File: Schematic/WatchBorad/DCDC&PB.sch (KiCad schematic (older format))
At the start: 21 parts, among them M1 Motor_DC, SW3 SW_Push, SW4 SW_Push, SW5 SW_Push, U10 TPS62740DSST, U9 MAX809STRG

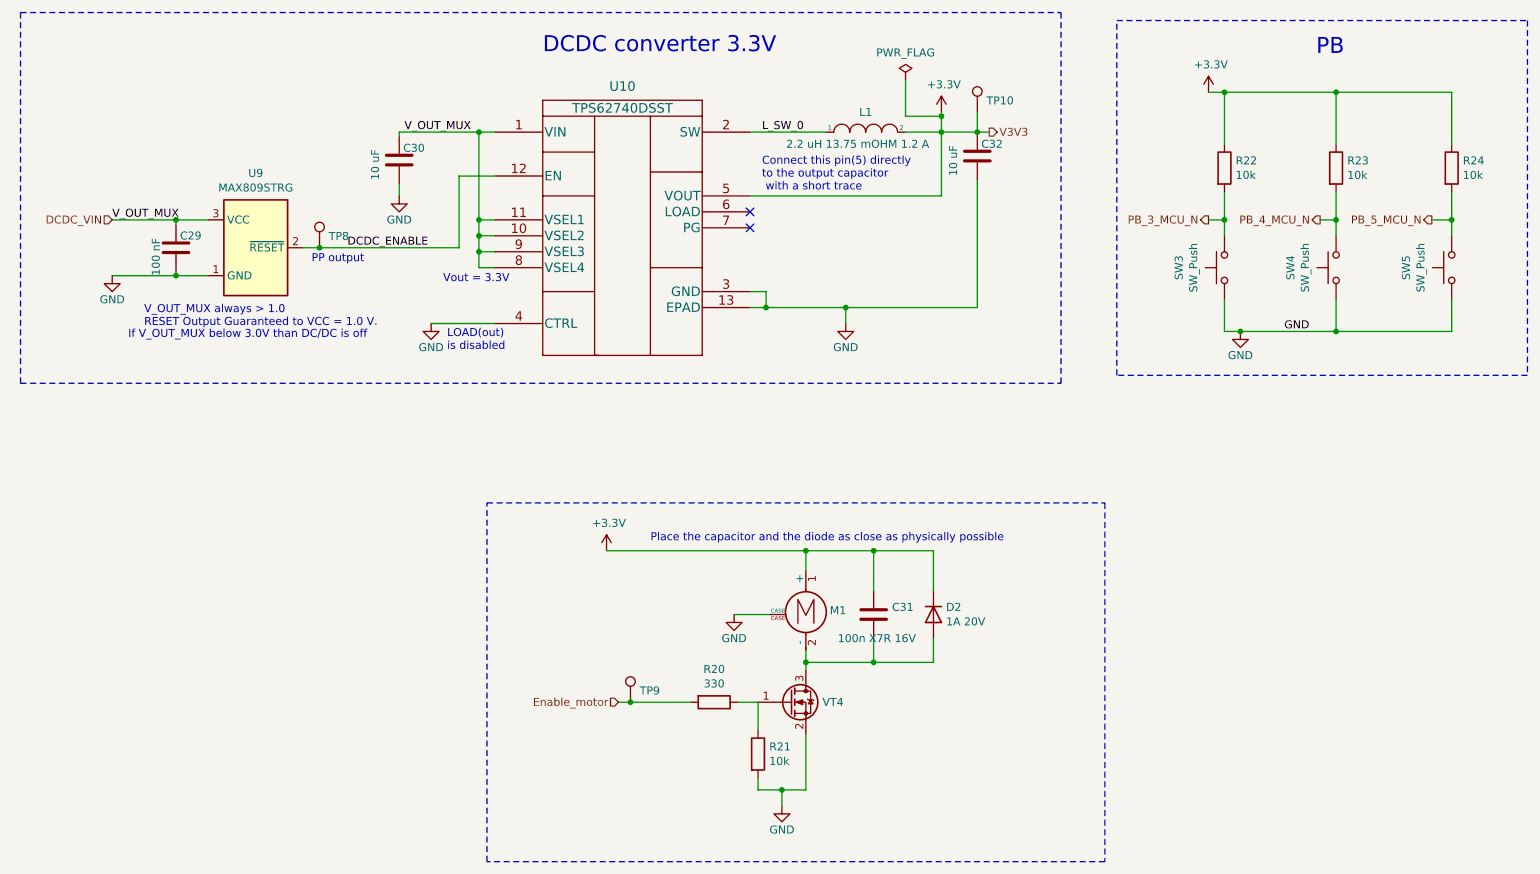
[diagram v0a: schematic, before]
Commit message: PBs are modified to one logic. Some minot changes
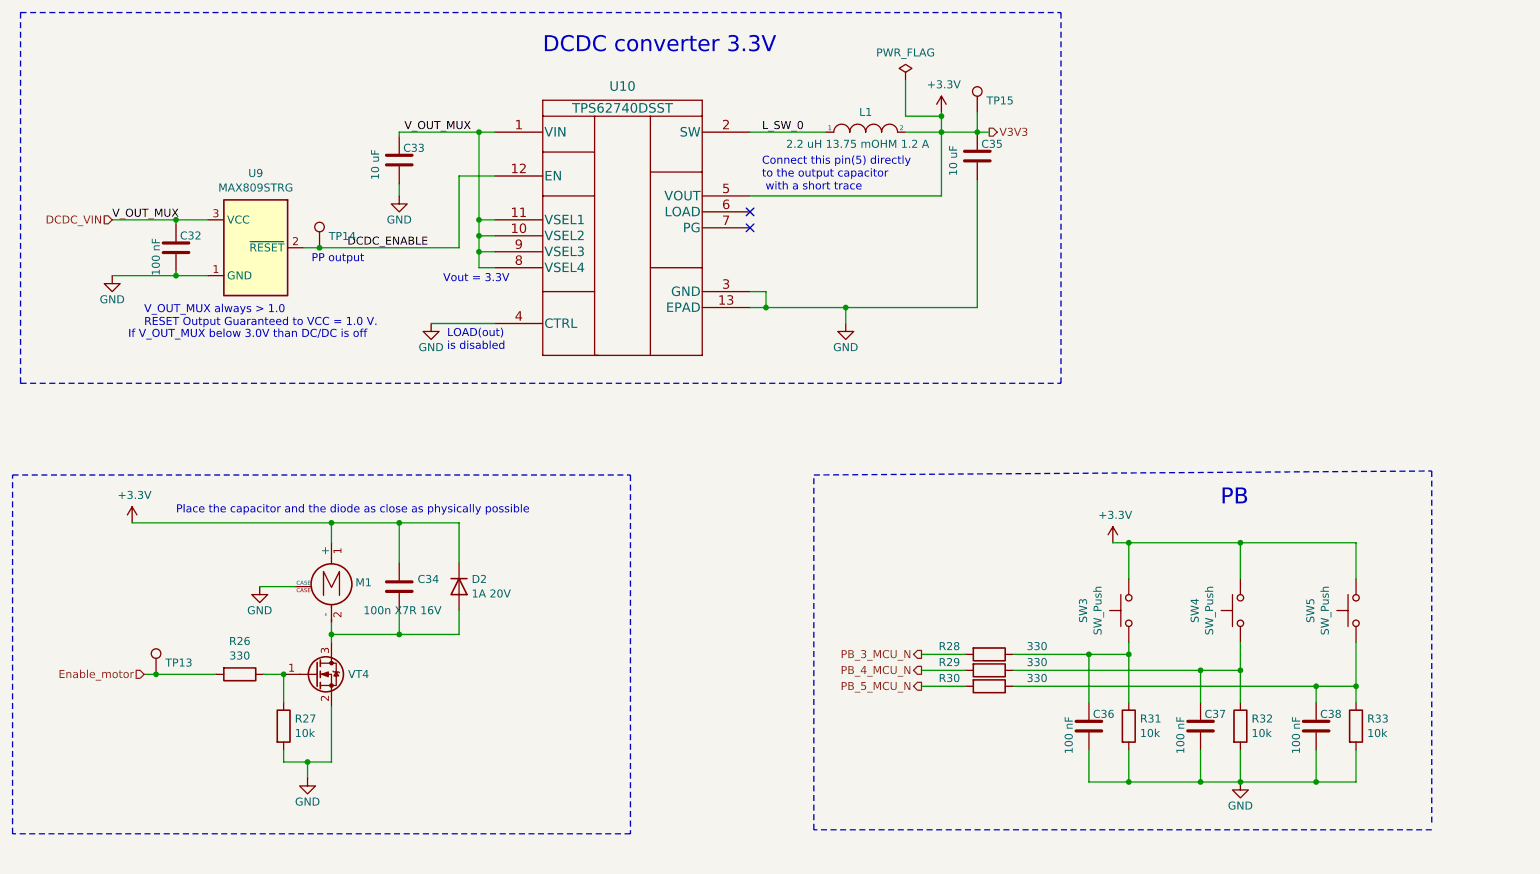
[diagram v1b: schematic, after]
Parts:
- added C36, C37, C38: 100 nF, Capacitors_SMD:C_0603_HandSoldering, symbol Device:C
- added R28, R29, R30: 330, Resistors_SMD:R_0603_HandSoldering, symbol Device:R
- renumbered C29 to C32, C30 to C33, C31 to C34, C32 to C35, R20 to R26, R21 to R27, R22 to R31, R23 to R32, R24 to R33, TP9 to TP13, TP8 to TP14, TP10 to TP15
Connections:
- net +3V3: now also SW3.2, SW4.2, SW5.2; no longer R31.1, R32.1, R33.1
- net GND: now also R31.2, R32.2, R33.2, C36.2, C37.2, C38.2; no longer SW3.1, SW4.1, SW5.1
- net PB_3_MCU_N: now also R28.2; no longer R31.2, SW3.2
- net PB_4_MCU_N: now also R29.2; no longer R32.2, SW4.2
- net PB_5_MCU_N: now also R30.2; no longer R33.2, SW5.2
- new net: C36.1, R28.1, R31.1, SW3.1
- new net: C37.1, R29.1, R32.1, SW4.1
- new net: C38.1, R30.1, R33.1, SW5.1
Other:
- moved on the sheet: C34, D2, M1, R26, R27, R31, R32, R33, SW3, SW4, SW5, TP13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

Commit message: Fixed LCSC schematic link :Schematic [SCHEMATIC]
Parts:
- C33, C35: LCSC https://lcsc.com/product-detail/Multilayer-Ceramic-Capacito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 -> (none); lcsc (none) -> https://lcsc.com/product-detail/Multilayer-Ceramic-Capacito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
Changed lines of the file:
@@
 AR Path="/5F7F86D0/5F9A3890" Ref="U?"  Part="1"
 AR Path="/5F988DA5/5F9A3890" Ref="U10"  Part="1"
+AR Path="/5F9A3890" Ref="U10"  Part="1"
 F 0 "U10" H 4800 2262 60  0000 C CNN
 F 1 "TPS62740DSST" H 4800 2125 60  0000 C CNN
@@
 F 2 "Capacitors_SMD:C_0603_HandSoldering" H 3438 1800 50  0001 C CNN
 F 3 "~" H 3400 1950 50  0001 C CNN
-F 4 "https://lcsc.com/product-detail/Multilayer-Ceramic-Capacitors-MLCC-SMD-SMT_SANYEAR-C0603X5R106M160NT_C466781.html" H 3400 1950 50  0001 C CNN "LCSC"
+F 4 "" H 3400 1950 50  0001 C CNN "LCSC"
+F 5 "https://lcsc.com/product-detail/Multilayer-Ceramic-Capacitors-MLCC-SMD-SMT_SANYEAR-C0603X5R106M160NT_C466781.html" H 3400 1950 50  0001 C CNN "lcsc"
 	1    3400 1950
 	1    0    0    -1
@@
 F 2 "Capacitors_SMD:C_0603_HandSoldering" H 7063 1775 50  0001 C CNN
 F 3 "~" H 7025 1925 50  0001 C CNN
-F 4 "https://lcsc.com/product-detail/Multilayer-Ceramic-Capacitors-MLCC-SMD-SMT_SANYEAR-C0603X5R106M160NT_C466781.html" H 7025 1925 50  0001 C CNN "LCSC"
+F 4 "" H 7025 1925 50  0001 C CNN "LCSC"
+F 5 "https://lcsc.com/product-detail/Multilayer-Ceramic-Capacitors-MLCC-SMD-SMT_SANYEAR-C0603X5R106M160NT_C466781.html" H 7025 1925 50  0001 C CNN "lcsc"
 	1    7025 1925
 	1    0    0    -1

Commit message: Added footpring for GC9A01 display. Fixed display lines(FMARK->DC)
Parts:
- U10: symbol DCDC_Local:TPS62740DSST -> WatchBorad-rescue:TPS62740DSST-DCDC_Local
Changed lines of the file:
@@
 $EndDescr
 $Comp
-L DCDC_Local:TPS62740DSST U?
+L WatchBorad-rescue:TPS62740DSST-DCDC_Local U?
 U 1 1 5F9A3890
 P 4000 1875

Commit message: Fixed components references for 0603 resistors and capacitors[SCHEMATIC]
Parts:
- C32, C33, C34, C35, C36, C37, C38: footprint Capacitors_SMD:C_0603_HandSoldering -> Capacitor_SMD:C_0603_1608Metric_Pad1.08x0.95mm_HandSolder
- R26, R27, R28, R29, R30, R31, R32, R33: footprint Resistors_SMD:R_0603_HandSoldering -> Resistor_SMD:R_0603_1608Metric_Pad0.98x0.95mm_HandSolder
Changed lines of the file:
@@
 F 0 "C33" H 3425 2025 50  0000 L CNN
 F 1 "10 uF" V 3250 1825 50  0000 L CNN
-F 2 "Capacitors_SMD:C_0603_HandSoldering" H 3438 1800 50  0001 C CNN
+F 2 "Capacitor_SMD:C_0603_1608Metric_Pad1.08x0.95mm_HandSolder" H 3438 1800 50  0001 C CNN
 F 3 "~" H 3400 1950 50  0001 C CNN
 F 4 "" H 3400 1950 50  0001 C CNN "LCSC"
@@
 F 0 "C35" H 7050 2000 50  0000 L CNN
 F 1 "10 uF" V 6875 1800 50  0000 L CNN
-F 2 "Capacitors_SMD:C_0603_HandSoldering" H 7063 1775 50  0001 C CNN
+F 2 "Capacitor_SMD:C_0603_1608Metric_Pad1.08x0.95mm_HandSolder" H 7063 1775 50  0001 C CNN
 F 3 "~" H 7025 1925 50  0001 C CNN
 F 4 "" H 7025 1925 50  0001 C CNN "LCSC"
@@
 F 0 "C32" H 2025 2575 50  0000 L CNN
 F 1 "100 nF" V 1875 2325 50  0000 L CNN
-F 2 "Capacitors_SMD:C_0603_HandSoldering" H 2038 2350 50  0001 C CNN
+F 2 "Capacitor_SMD:C_0603_1608Metric_Pad1.08x0.95mm_HandSolder" H 2038 2350 50  0001 C CNN
 F 3 "~" H 2000 2500 50  0001 C CNN
 	1    2000 2500
@@
 F 0 "R31" H 8045 5546 50  0000 L CNN
 F 1 "10k" H 8045 5455 50  0000 L CNN
-F 2 "Resistors_SMD:R_0603_HandSoldering" V 7905 5500 50  0001 C CNN
+F 2 "Resistor_SMD:R_0603_1608Metric_Pad0.98x0.95mm_HandSolder" V 7905 5500 50  0001 C CNN
 F 3 "~" H 7975 5500 50  0001 C CNN
 	1    7975 5500
@@
 F 0 "R32" H 8745 5546 50  0000 L CNN
 F 1 "10k" H 8745 5455 50  0000 L CNN
-F 2 "Resistors_SMD:R_0603_HandSoldering" V 8605 5500 50  0001 C CNN
+F 2 "Resistor_SMD:R_0603_1608Metric_Pad0.98x0.95mm_HandSolder" V 8605 5500 50  0001 C CNN
 F 3 "~" H 8675 5500 50  0001 C CNN
 	1    8675 5500
@@
 F 0 "R33" H 9470 5546 50  0000 L CNN
 F 1 "10k" H 9470 5455 50  0000 L CNN
-F 2 "Resistors_SMD:R_0603_HandSoldering" V 9330 5500 50  0001 C CNN
+F 2 "Resistor_SMD:R_0603_1608Metric_Pad0.98x0.95mm_HandSolder" V 9330 5500 50  0001 C CNN
 F 3 "~" H 9400 5500 50  0001 C CNN
 	1    9400 5500
@@
 F 0 "R27" H 2745 5546 50  0000 L CNN
 F 1 "10k" H 2745 5455 50  0000 L CNN
-F 2 "Resistors_SMD:R_0603_HandSoldering" V 2605 5500 50  0001 C CNN
+F 2 "Resistor_SMD:R_0603_1608Metric_Pad0.98x0.95mm_HandSolder" V 2605 5500 50  0001 C CNN
 F 3 "~" H 2675 5500 50  0001 C CNN
 	1    2675 5500
@@
 F 0 "R26" V 2193 5175 50  0000 C CNN
 F 1 "330" V 2284 5175 50  0000 C CNN
-F 2 "Resistors_SMD:R_0603_HandSoldering" V 2330 5175 50  0001 C CNN
+F 2 "Resistor_SMD:R_0603_1608Metric_Pad0.98x0.95mm_HandSolder" V 2330 5175 50  0001 C CNN
 F 3 "https://lcsc.com/product-detail/Others_Viking-Tech-ARG03FTC3300_C217969.html" H 2400 5175 50  0001 C CNN
 	1    2400 5175
@@
 F 0 "C34" H 3515 4671 50  0000 L CNN
 F 1 "100n X7R 16V" H 3175 4475 50  0000 L CNN
-F 2 "Capacitors_SMD:C_0603_HandSoldering" H 3438 4475 50  0001 C CNN
+F 2 "Capacitor_SMD:C_0603_1608Metric_Pad1.08x0.95mm_HandSolder" H 3438 4475 50  0001 C CNN
 F 3 "~" H 3400 4625 50  0001 C CNN
 	1    3400 4625
@@
 F 0 "R28" V 7050 4800 50  0000 C CNN
 F 1 "330" V 7050 5350 50  0000 C CNN
-F 2 "Resistors_SMD:R_0603_HandSoldering" V 7030 5050 50  0001 C CNN
+F 2 "Resistor_SMD:R_0603_1608Metric_Pad0.98x0.95mm_HandSolder" V 7030 5050 50  0001 C CNN
 F 3 "https://lcsc.com/product-detail/Others_Viking-Tech-ARG03FTC3300_C217969.html" H 7100 5050 50  0001 C CNN
 	1    7100 5050
@@
 F 0 "R29" V 7050 4900 50  0000 C CNN
 F 1 "330" V 7050 5450 50  0000 C CNN
-F 2 "Resistors_SMD:R_0603_HandSoldering" V 7030 5150 50  0001 C CNN
+F 2 "Resistor_SMD:R_0603_1608Metric_Pad0.98x0.95mm_HandSolder" V 7030 5150 50  0001 C CNN
 F 3 "https://lcsc.com/product-detail/Others_Viking-Tech-ARG03FTC3300_C217969.html" H 7100 5150 50  0001 C CNN
 	1    7100 5150
@@
 F 0 "R30" V 7050 5000 50  0000 C CNN
 F 1 "330" V 7050 5550 50  0000 C CNN
-F 2 "Resistors_SMD:R_0603_HandSoldering" V 7030 5250 50  0001 C CNN
+F 2 "Resistor_SMD:R_0603_1608Metric_Pad0.98x0.95mm_HandSolder" V 7030 5250 50  0001 C CNN
 F 3 "https://lcsc.com/product-detail/Others_Viking-Tech-ARG03FTC3300_C217969.html" H 7100 5250 50  0001 C CNN
 	1    7100 5250
@@
 F 0 "C36" H 7750 5575 50  0000 L CNN
 F 1 "100 nF" V 7600 5325 50  0000 L CNN
-F 2 "Capacitors_SMD:C_0603_HandSoldering" H 7763 5350 50  0001 C CNN
+F 2 "Capacitor_SMD:C_0603_1608Metric_Pad1.08x0.95mm_HandSolder" H 7763 5350 50  0001 C CNN
 F 3 "~" H 7725 5500 50  0001 C CNN
 	1    7725 5500
@@
 F 0 "C37" H 8450 5575 50  0000 L CNN
 F 1 "100 nF" V 8300 5325 50  0000 L CNN
-F 2 "Capacitors_SMD:C_0603_HandSoldering" H 8463 5350 50  0001 C CNN
+F 2 "Capacitor_SMD:C_0603_1608Metric_Pad1.08x0.95mm_HandSolder" H 8463 5350 50  0001 C CNN
 F 3 "~" H 8425 5500 50  0001 C CNN
 	1    8425 5500
@@
 F 0 "C38" H 9175 5575 50  0000 L CNN
 F 1 "100 nF" V 9025 5325 50  0000 L CNN
-F 2 "Capacitors_SMD:C_0603_HandSoldering" H 9188 5350 50  0001 C CNN
+F 2 "Capacitor_SMD:C_0603_1608Metric_Pad1.08x0.95mm_HandSolder" H 9188 5350 50  0001 C CNN
 F 3 "~" H 9150 5500 50  0001 C CNN
 	1    9150 5500

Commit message: Updated 0603 components from hand-solder version to fabrical
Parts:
- C32, C33, C34, C35, C36, C37, C38: footprint Capacitor_SMD:C_0603_1608Metric_Pad1.08x0.95mm_HandSolder -> Capacitor_SMD:C_0603_1608Metric
- R26, R27, R28, R29, R30, R31, R32, R33: footprint Resistor_SMD:R_0603_1608Metric_Pad0.98x0.95mm_HandSolder -> Resistor_SMD:R_0603_1608Metric
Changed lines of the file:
@@
 F 0 "C33" H 3425 2025 50  0000 L CNN
 F 1 "10 uF" V 3250 1825 50  0000 L CNN
-F 2 "Capacitor_SMD:C_0603_1608Metric_Pad1.08x0.95mm_HandSolder" H 3438 1800 50  0001 C CNN
+F 2 "Capacitor_SMD:C_0603_1608Metric" H 3438 1800 50  0001 C CNN
 F 3 "~" H 3400 1950 50  0001 C CNN
 F 4 "" H 3400 1950 50  0001 C CNN "LCSC"
@@
 F 0 "C35" H 7050 2000 50  0000 L CNN
 F 1 "10 uF" V 6875 1800 50  0000 L CNN
-F 2 "Capacitor_SMD:C_0603_1608Metric_Pad1.08x0.95mm_HandSolder" H 7063 1775 50  0001 C CNN
+F 2 "Capacitor_SMD:C_0603_1608Metric" H 7063 1775 50  0001 C CNN
 F 3 "~" H 7025 1925 50  0001 C CNN
 F 4 "" H 7025 1925 50  0001 C CNN "LCSC"
@@
 F 0 "C32" H 2025 2575 50  0000 L CNN
 F 1 "100 nF" V 1875 2325 50  0000 L CNN
-F 2 "Capacitor_SMD:C_0603_1608Metric_Pad1.08x0.95mm_HandSolder" H 2038 2350 50  0001 C CNN
+F 2 "Capacitor_SMD:C_0603_1608Metric" H 2038 2350 50  0001 C CNN
 F 3 "~" H 2000 2500 50  0001 C CNN
 	1    2000 2500
@@
 F 0 "R31" H 8045 5546 50  0000 L CNN
 F 1 "10k" H 8045 5455 50  0000 L CNN
-F 2 "Resistor_SMD:R_0603_1608Metric_Pad0.98x0.95mm_HandSolder" V 7905 5500 50  0001 C CNN
+F 2 "Resistor_SMD:R_0603_1608Metric" V 7905 5500 50  0001 C CNN
 F 3 "~" H 7975 5500 50  0001 C CNN
 	1    7975 5500
@@
 F 0 "R32" H 8745 5546 50  0000 L CNN
 F 1 "10k" H 8745 5455 50  0000 L CNN
-F 2 "Resistor_SMD:R_0603_1608Metric_Pad0.98x0.95mm_HandSolder" V 8605 5500 50  0001 C CNN
+F 2 "Resistor_SMD:R_0603_1608Metric" V 8605 5500 50  0001 C CNN
 F 3 "~" H 8675 5500 50  0001 C CNN
 	1    8675 5500
@@
 F 0 "R33" H 9470 5546 50  0000 L CNN
 F 1 "10k" H 9470 5455 50  0000 L CNN
-F 2 "Resistor_SMD:R_0603_1608Metric_Pad0.98x0.95mm_HandSolder" V 9330 5500 50  0001 C CNN
+F 2 "Resistor_SMD:R_0603_1608Metric" V 9330 5500 50  0001 C CNN
 F 3 "~" H 9400 5500 50  0001 C CNN
 	1    9400 5500
@@
 F 0 "R27" H 2745 5546 50  0000 L CNN
 F 1 "10k" H 2745 5455 50  0000 L CNN
-F 2 "Resistor_SMD:R_0603_1608Metric_Pad0.98x0.95mm_HandSolder" V 2605 5500 50  0001 C CNN
+F 2 "Resistor_SMD:R_0603_1608Metric" V 2605 5500 50  0001 C CNN
 F 3 "~" H 2675 5500 50  0001 C CNN
 	1    2675 5500
@@
 F 0 "R26" V 2193 5175 50  0000 C CNN
 F 1 "330" V 2284 5175 50  0000 C CNN
-F 2 "Resistor_SMD:R_0603_1608Metric_Pad0.98x0.95mm_HandSolder" V 2330 5175 50  0001 C CNN
+F 2 "Resistor_SMD:R_0603_1608Metric" V 2330 5175 50  0001 C CNN
 F 3 "https://lcsc.com/product-detail/Others_Viking-Tech-ARG03FTC3300_C217969.html" H 2400 5175 50  0001 C CNN
 	1    2400 5175
@@
 F 0 "C34" H 3515 4671 50  0000 L CNN
 F 1 "100n X7R 16V" H 3175 4475 50  0000 L CNN
-F 2 "Capacitor_SMD:C_0603_1608Metric_Pad1.08x0.95mm_HandSolder" H 3438 4475 50  0001 C CNN
+F 2 "Capacitor_SMD:C_0603_1608Metric" H 3438 4475 50  0001 C CNN
 F 3 "~" H 3400 4625 50  0001 C CNN
 	1    3400 4625
@@
 F 0 "R28" V 7050 4800 50  0000 C CNN
 F 1 "330" V 7050 5350 50  0000 C CNN
-F 2 "Resistor_SMD:R_0603_1608Metric_Pad0.98x0.95mm_HandSolder" V 7030 5050 50  0001 C CNN
+F 2 "Resistor_SMD:R_0603_1608Metric" V 7030 5050 50  0001 C CNN
 F 3 "https://lcsc.com/product-detail/Others_Viking-Tech-ARG03FTC3300_C217969.html" H 7100 5050 50  0001 C CNN
 	1    7100 5050
@@
 F 0 "R29" V 7050 4900 50  0000 C CNN
 F 1 "330" V 7050 5450 50  0000 C CNN
-F 2 "Resistor_SMD:R_0603_1608Metric_Pad0.98x0.95mm_HandSolder" V 7030 5150 50  0001 C CNN
+F 2 "Resistor_SMD:R_0603_1608Metric" V 7030 5150 50  0001 C CNN
 F 3 "https://lcsc.com/product-detail/Others_Viking-Tech-ARG03FTC3300_C217969.html" H 7100 5150 50  0001 C CNN
 	1    7100 5150
@@
 F 0 "R30" V 7050 5000 50  0000 C CNN
 F 1 "330" V 7050 5550 50  0000 C CNN
-F 2 "Resistor_SMD:R_0603_1608Metric_Pad0.98x0.95mm_HandSolder" V 7030 5250 50  0001 C CNN
+F 2 "Resistor_SMD:R_0603_1608Metric" V 7030 5250 50  0001 C CNN
 F 3 "https://lcsc.com/product-detail/Others_Viking-Tech-ARG03FTC3300_C217969.html" H 7100 5250 50  0001 C CNN
 	1    7100 5250
@@
 F 0 "C36" H 7750 5575 50  0000 L CNN
 F 1 "100 nF" V 7600 5325 50  0000 L CNN
-F 2 "Capacitor_SMD:C_0603_1608Metric_Pad1.08x0.95mm_HandSolder" H 7763 5350 50  0001 C CNN
+F 2 "Capacitor_SMD:C_0603_1608Metric" H 7763 5350 50  0001 C CNN
 F 3 "~" H 7725 5500 50  0001 C CNN
 	1    7725 5500
@@
 F 0 "C37" H 8450 5575 50  0000 L CNN
 F 1 "100 nF" V 8300 5325 50  0000 L CNN
-F 2 "Capacitor_SMD:C_0603_1608Metric_Pad1.08x0.95mm_HandSolder" H 8463 5350 50  0001 C CNN
+F 2 "Capacitor_SMD:C_0603_1608Metric" H 8463 5350 50  0001 C CNN
 F 3 "~" H 8425 5500 50  0001 C CNN
 	1    8425 5500
@@
 F 0 "C38" H 9175 5575 50  0000 L CNN
 F 1 "100 nF" V 9025 5325 50  0000 L CNN
-F 2 "Capacitor_SMD:C_0603_1608Metric_Pad1.08x0.95mm_HandSolder" H 9188 5350 50  0001 C CNN
+F 2 "Capacitor_SMD:C_0603_1608Metric" H 9188 5350 50  0001 C CNN
 F 3 "~" H 9150 5500 50  0001 C CNN
 	1    9150 5500

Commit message: Updated parts list accroding to the Ruslan fixes
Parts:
- D2: lcsc https://lcsc.com/product-detail/Schottky-Barrier-Diodes-SBD_Shandong-Jingdao-Microelectronics-SS12_C353243.html -> https://lcsc.com/product-detail/Schottky-Barrier-Diodes-SBD_Slkor-SLKORMICRO-Elec-SS12_C513476.html
- SW3, SW4, SW5: footprint Buttons_Switches_SMD:SW_SPST_B3U-3000P-B -> OmronSwitch:SW_B3U-3000P; lcsc https://lcsc.com/products/Tactile-Switches_427.html?q=b3u-3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 -> https://lcsc.com/product-detail/Tactile-Switches_Omron-Elec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
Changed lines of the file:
@@
 F 0 "SW3" H 7975 5060 50  0000 C CNN
 F 1 "SW_Push" H 7975 4969 50  0000 C CNN
-F 2 "Buttons_Switches_SMD:SW_SPST_B3U-3000P-B" H 7975 4975 50  0001 C CNN
-F 3 "https://datasheet.lcsc.com/szlcsc/Omron-Electronics-B3U-3000PM-B_C306884.pdf" H 7975 4975 50  0001 C CNN
-F 4 "https://lcsc.com/products/Tactile-Switches_427.html?q=b3u-3000" H 7975 4775 50  0001 C CNN "lcsc"
+F 2 "OmronSwitch:SW_B3U-3000P" H 7975 4975 50  0001 C CNN
+F 3 "https://datasheet.lcsc.com/lcsc/2012042009_Omron-Electronics-B3U-3000P_C963349.pdf" H 7975 4975 50  0001 C CNN
+F 4 "https://lcsc.com/product-detail/Tactile-Switches_Omron-Electronics-B3U-3000P_C963349.html" H 7975 4775 50  0001 C CNN "lcsc"
 	1    7975 4775
 	0    -1   -1   0
@@
 F 0 "SW4" H 8675 5060 50  0000 C CNN
 F 1 "SW_Push" H 8675 4969 50  0000 C CNN
-F 2 "Buttons_Switches_SMD:SW_SPST_B3U-3000P-B" H 8675 4975 50  0001 C CNN
-F 3 "https://datasheet.lcsc.com/szlcsc/Omron-Electronics-B3U-3000PM-B_C306884.pdf" H 8675 4975 50  0001 C CNN
-F 4 "https://lcsc.com/products/Tactile-Switches_427.html?q=b3u-3000" H 8675 4775 50  0001 C CNN "lcsc"
+F 2 "OmronSwitch:SW_B3U-3000P" H 8675 4975 50  0001 C CNN
+F 3 "https://datasheet.lcsc.com/lcsc/2012042009_Omron-Electronics-B3U-3000P_C963349.pdf" H 8675 4975 50  0001 C CNN
+F 4 "https://lcsc.com/product-detail/Tactile-Switches_Omron-Electronics-B3U-3000P_C963349.html" H 8675 4775 50  0001 C CNN "lcsc"
 	1    8675 4775
 	0    -1   -1   0
@@
 F 0 "SW5" H 9400 5060 50  0000 C CNN
 F 1 "SW_Push" H 9400 4969 50  0000 C CNN
-F 2 "Buttons_Switches_SMD:SW_SPST_B3U-3000P-B" H 9400 4975 50  0001 C CNN
-F 3 "https://datasheet.lcsc.com/szlcsc/Omron-Electronics-B3U-3000PM-B_C306884.pdf" H 9400 4975 50  0001 C CNN
-F 4 "https://lcsc.com/products/Tactile-Switches_427.html?q=b3u-3000" H 9400 4775 50  0001 C CNN "lcsc"
+F 2 "OmronSwitch:SW_B3U-3000P" H 9400 4975 50  0001 C CNN
+F 3 "https://datasheet.lcsc.com/lcsc/2012042009_Omron-Electronics-B3U-3000P_C963349.pdf" H 9400 4975 50  0001 C CNN
+F 4 "https://lcsc.com/product-detail/Tactile-Switches_Omron-Electronics-B3U-3000P_C963349.html" H 9400 4775 50  0001 C CNN "lcsc"
 	1    9400 4775
 	0    -1   -1   0
@@
 F 1 "1A 20V" V 3820 4704 50  0000 L CNN
 F 2 "Diodes_SMD:D_SMA_Handsoldering" H 3775 4625 50  0001 C CNN
-F 3 "https://datasheet.lcsc.com/szlcsc/1901021833_Shandong-Jingdao-Microelectronics-SS12_C353243.pdf" H 3775 4625 50  0001 C CNN
-F 4 "https://lcsc.com/product-detail/Schottky-Barrier-Diodes-SBD_Shandong-Jingdao-Microelectronics-SS12_C353243.html" V 3775 4625 50  0001 C CNN "lcsc"
+F 3 "https://datasheet.lcsc.com/lcsc/2004140934_Slkor-SLKORMICRO-Elec-SS12_C513476.pdf" H 3775 4625 50  0001 C CNN
+F 4 "https://lcsc.com/product-detail/Schottky-Barrier-Diodes-SBD_Slkor-SLKORMICRO-Elec-SS12_C513476.html" V 3775 4625 50  0001 C CNN "lcsc"
 	1    3775 4625
 	0    1    1    0
